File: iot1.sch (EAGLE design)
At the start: 10 parts, among them U2 HTU21D

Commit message: adding MEGA8-P controller
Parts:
- added C2, C3, C4: (no value), rcl:C-EU050-025X075
- added IC1: MEGA8-P, atmel:MEGA8-P
- added Q1: (no value), crystal:CRYSTALHC18U-V
- added R3, R4: (no value), rcl:R-EU_0204/7
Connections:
- new net 5V: C2.1, IC1.VCC@1, R3.2
- new net N$15: IC1.PC0(ADC0)
- new net N$16: IC1.PC1(ADC1)
- new net N$22: IC1.PC2(ADC2)
- new net N$23: IC1.PC3(ADC3)
- new net N$29: IC1.PC4(ADC4/SDA)
- new net N$31: IC1.PC5(ADC5/SCL)
- new net N$41: IC1.PD0(RXD)
- new net N$42: IC1.PD1(TXD)
- new net N$43: IC1.PD2(INT0)
- new net N$44: IC1.PD3(INT1)
- new net N$45: IC1.PD4(XCK/T0)
- new net N$58: IC1.PD5(T1)
- new net N$59: IC1.PD6(AIN0)
- new net N$60: IC1.PD7(AIN1)
- new net N$61: IC1.PB0(ICP)
- new net N$62: IC1.PB1(OC1A)
- new net N$63: IC1.PB2(SS/OC1B)
- new net N$64: IC1.PB3(MOSI/OC2)
- new net N$65: IC1.PB4(MISO)
- new net N$66: IC1.PB5(SCK)
- new net N$67: IC1.PC6(/RESET), R3.1
- new net N$68: IC1.GND
- new net N$69: IC1.AREF
- new net N$70: IC1.AVCC
- new net N$72: C4.2, IC1.PB7(XTAL2/TOSC2), Q1.1, R4.1
- new net N$73: C3.2, IC1.PB6(XTAL1/TOSC1), Q1.2, R4.2
- net GND: now also C2.2, C3.1, C4.1, IC1.GND@1

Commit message: adding moisture input and adding voltage regulator
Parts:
- added IC2: 7805T, linear:7805T
- added X1: 22-23-2041, con-molex:22-23-2041
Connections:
- removed net N$65: IC1.PB4(MISO)
- removed net N$66: IC1.PB5(SCK)
- new net SOIL_MOISTURE_0: X1-1.S
- new net SOIL_MOISTURE_1: X1-3.S
- new net V_IN: IC2.VI
- net 5V: now also IC2.VO
- net GND: now also IC2.GND, X1-2.S, X1-4.S
- net RX: now also IC1.PB4(MISO)
- net TX: now also IC1.PB5(SCK)
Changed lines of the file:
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@@
 <part name="C3" library="rcl" library_urn="urn:adsk.eagle:library:334" deviceset="C-EU" device="050-025X075" package3d_urn="urn:adsk.eagle:package:23637/1"/>
 <part name="C4" library="rcl" library_urn="urn:adsk.eagle:library:334" deviceset="C-EU" device="050-025X075" package3d_urn="urn:adsk.eagle:package:23637/1"/>
+<part name="FRAME4" library="frames" library_urn="urn:adsk.eagle:library:229" deviceset="A4L-LOC" device=""/>
+<part name="X1" library="con-molex" library_urn="urn:adsk.eagle:library:165" deviceset="22-23-2041" device="" package3d_urn="urn:adsk.eagle:package:8078635/1"/>
+<part name="IC2" library="linear" library_urn="urn:adsk.eagle:library:262" deviceset="78*" device="T" package3d_urn="urn:adsk.eagle:package:16414/1" technology="05"/>
 </parts>
 <sheets>
@@
 </segment>
 </net>
-<net name="N$65" class="0">
+<net name="RX" class="0">
 <segment>
 <pinref part="IC1" gate="G$1" pin="PB4(MISO)"/>
 <wire x1="162.56" y1="109.22" x2="187.96" y2="109.22" width="0.1524" layer="91"/>
-</segment>
-</net>
-<net name="N$66" class="0">
+<label x="190.5" y="109.22" size="1.778" layer="95"/>
+</segment>
+</net>
+<net name="TX" class="0">
 <segment>
 <pinref part="IC1" gate="G$1" pin="PB5(SCK)"/>
 <wire x1="162.56" y1="106.68" x2="187.96" y2="106.68" width="0.1524" layer="91"/>
+<label x="190.5" y="106.68" size="1.778" layer="95"/>
 </segment>
 </net>
@@
 </segment>
 </net>
+</nets>
+</sheet>
+<sheet>
+<plain>
+</plain>
+<instances>
+<instance part="FRAME4" gate="G$1" x="-5.08" y="10.16" smashed="yes">
+<attribute name="DRAWING_NAME" x="212.09" y="25.4" size="2.54" layer="94"/>
+<attribute name="LAST_DATE_TIME" x="212.09" y="20.32" size="2.286" layer="94"/>
+<attribute name="SHEET" x="225.425" y="15.24" size="2.54" layer="94"/>
+</instance>
+<instance part="X1" gate="-1" x="190.5" y="121.92" smashed="yes">
+<attribute name="NAME" x="193.04" y="121.158" size="1.524" layer="95"/>
+<attribute name="VALUE" x="189.738" y="123.317" size="1.778" layer="96"/>
+</instance>
+<instance part="X1" gate="-2" x="190.5" y="119.38" smashed="yes">
+<attribute name="NAME" x="193.04" y="118.618" size="1.524" layer="95"/>
+</instance>
+<instance part="X1" gate="-3" x="190.5" y="116.84" smashed="yes">
+<attribute name="NAME" x="193.04" y="116.078" size="1.524" layer="95"/>
+</instance>
+<instance part="X1" gate="-4" x="190.5" y="114.3" smashed="yes">
+<attribute name="NAME" x="193.04" y="113.538" size="1.524" layer="95"/>
+</instance>
+<instance part="IC2" gate="A1" x="55.88" y="142.24" smashed="yes">
+<attribute name="NAME" x="48.26" y="147.955" size="1.778" layer="95"/>
+<attribute name="VALUE" x="48.26" y="145.415" size="1.778" layer="96"/>
+</instance>
+</instances>
+<busses>
+</busses>
+<nets>
+<net name="SOIL_MOISTURE_0" class="0">
+<segment>
+<pinref part="X1" gate="-1" pin="S"/>
+<wire x1="187.96" y1="121.92" x2="177.8" y2="121.92" width="0.1524" layer="91"/>
+<label x="152.4" y="121.92" size="1.778" layer="95"/>
+</segment>
+</net>
+<net name="GND" class="0">
+<segment>
+<pinref part="X1" gate="-2" pin="S"/>
+<wire x1="187.96" y1="119.38" x2="177.8" y2="119.38" width="0.1524" layer="91"/>
+<label x="170.18" y="119.38" size="1.778" layer="95"/>
+</segment>
+<segment>
+<pinref part="X1" gate="-4" pin="S"/>
+<wire x1="187.96" y1="114.3" x2="177.8" y2="114.3" width="0.1524" layer="91"/>
+<label x="170.18" y="114.3" size="1.778" layer="95"/>
+</segment>
+<segment>
+<pinref part="IC2" gate="A1" pin="GND"/>
+<wire x1="55.88" y1="134.62" x2="55.88" y2="129.54" width="0.1524" layer="91"/>
+<label x="55.88" y="127" size="1.778" layer="95"/>
+</segment>
+</net>
+<net name="SOIL_MOISTURE_1" class="0">
+<segment>
+<pinref part="X1" gate="-3" pin="S"/>
+<wire x1="187.96" y1="116.84" x2="177.8" y2="116.84" width="0.1524" layer="91"/>
+<label x="152.4" y="116.84" size="1.778" layer="95"/>
+</segment>
+</net>
+<net name="V_IN" class="0">
+<segment>
+<pinref part="IC2" gate="A1" pin="VI"/>
+<wire x1="45.72" y1="142.24" x2="43.18" y2="142.24" width="0.1524" layer="91"/>
+<label x="35.56" y="142.24" size="1.778" layer="95"/>
+</segment>
+</net>
+<net name="5V" class="0">
+<segment>
+<pinref part="IC2" gate="A1" pin="VO"/>
+<wire x1="66.04" y1="142.24" x2="71.12" y2="142.24" width="0.1524" layer="91"/>
+<label x="73.66" y="142.24" size="1.778" layer="95"/>
+</segment>
+</net>

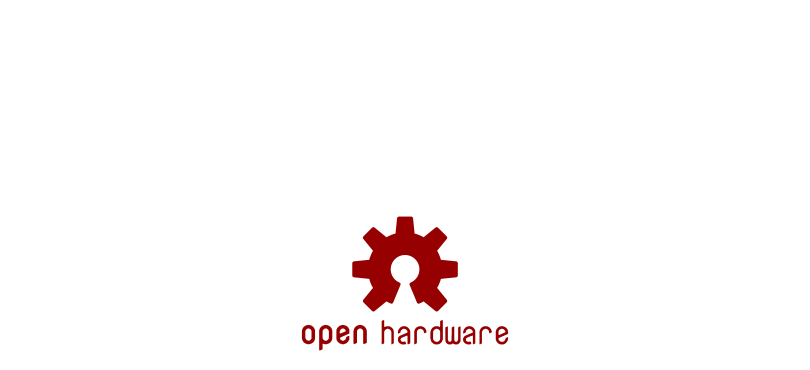
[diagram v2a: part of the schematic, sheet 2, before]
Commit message: adding power supply
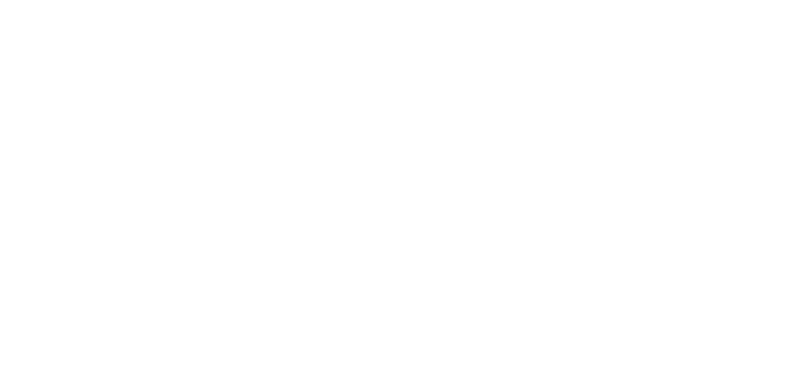
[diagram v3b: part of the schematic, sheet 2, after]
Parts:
- removed LOGO2: OSHW-LOGOS, SparkFun-Aesthetics:OSHW-LOGOS
- added C5, C6: (no value), rcl:CPOL-EUE1.8-4
- added J1: DCJ0202, con-jack:DCJ0202
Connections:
- net 5V: now also C6.+
- net GND: now also C5.-, C6.-, J1.2, J1.3
- net V_IN: now also C5.+, J1.1
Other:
- moved on the sheet: IC2
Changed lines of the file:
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@@
 <part name="GND4" library="SparkFun" deviceset="GND" device=""/>
 <part name="U2" library="SparkFun-Sensors" deviceset="HTU21D" device="SMD" value="HTU21D"/>
-<part name="LOGO2" library="SparkFun-Aesthetics" deviceset="OSHW-LOGO" device="S"/>
 <part name="JP1" library="SparkFun-Connectors" deviceset="M04" device="PTH"/>
 <part name="GND2" library="SparkFun" deviceset="GND" device=""/>
@@
 <part name="X1" library="con-molex" library_urn="urn:adsk.eagle:library:165" deviceset="22-23-2041" device="" package3d_urn="urn:adsk.eagle:package:8078635/1"/>
 <part name="IC2" library="linear" library_urn="urn:adsk.eagle:library:262" deviceset="78*" device="T" package3d_urn="urn:adsk.eagle:package:16414/1" technology="05"/>
+<part name="J1" library="con-jack" library_urn="urn:adsk.eagle:library:154" deviceset="DCJ0202" device="" package3d_urn="urn:adsk.eagle:package:7491/1"/>
+<part name="C5" library="rcl" library_urn="urn:adsk.eagle:library:334" deviceset="CPOL-EU" device="E1.8-4" package3d_urn="urn:adsk.eagle:package:23336/2"/>
+<part name="C6" library="rcl" library_urn="urn:adsk.eagle:library:334" deviceset="CPOL-EU" device="E1.8-4" package3d_urn="urn:adsk.eagle:package:23336/2"/>
 </parts>
 <sheets>
@@
 <attribute name="VALUE" x="139.7" y="78.74" size="1.778" layer="95"/>
 </instance>
-<instance part="LOGO2" gate="G$1" x="134.62" y="10.16" smashed="yes"/>
 <instance part="JP1" gate="G$1" x="73.66" y="96.52" smashed="yes" rot="MR180">
 <attribute name="VALUE" x="68.58" y="104.14" size="1.778" layer="96" rot="MR180"/>
@@
 <attribute name="NAME" x="193.04" y="113.538" size="1.524" layer="95"/>
 </instance>
-<instance part="IC2" gate="A1" x="55.88" y="142.24" smashed="yes">
-<attribute name="NAME" x="48.26" y="147.955" size="1.778" layer="95"/>
-<attribute name="VALUE" x="48.26" y="145.415" size="1.778" layer="96"/>
+<instance part="IC2" gate="A1" x="50.8" y="142.24" smashed="yes">
+<attribute name="NAME" x="43.18" y="147.955" size="1.778" layer="95"/>
+<attribute name="VALUE" x="43.18" y="145.415" size="1.778" layer="96"/>
+</instance>
+<instance part="J1" gate="G$1" x="12.7" y="139.7" smashed="yes">
+<attribute name="NAME" x="10.16" y="143.51" size="1.778" layer="95"/>
+<attribute name="VALUE" x="10.16" y="133.35" size="1.778" layer="96"/>
+</instance>
+<instance part="C5" gate="G$1" x="33.02" y="137.16" smashed="yes">
+<attribute name="NAME" x="34.163" y="137.6426" size="1.778" layer="95"/>
+<attribute name="VALUE" x="34.163" y="132.5626" size="1.778" layer="96"/>
+</instance>
+<instance part="C6" gate="G$1" x="68.58" y="134.62" smashed="yes">
+<attribute name="NAME" x="69.723" y="135.1026" size="1.778" layer="95"/>
+<attribute name="VALUE" x="69.723" y="130.0226" size="1.778" layer="96"/>
 </instance>
 </instances>
@@
 <segment>
 <pinref part="IC2" gate="A1" pin="GND"/>
-<wire x1="55.88" y1="134.62" x2="55.88" y2="129.54" width="0.1524" layer="91"/>
-<label x="55.88" y="127" size="1.778" layer="95"/>
+<wire x1="50.8" y1="134.62" x2="50.8" y2="127" width="0.1524" layer="91"/>
+<label x="55.88" y="124.46" size="1.778" layer="95"/>
+<wire x1="25.4" y1="127" x2="33.02" y2="127" width="0.1524" layer="91"/>
+<pinref part="C5" gate="G$1" pin="-"/>
+<wire x1="33.02" y1="127" x2="33.02" y2="132.08" width="0.1524" layer="91"/>
+<wire x1="33.02" y1="127" x2="50.8" y2="127" width="0.1524" layer="91"/>
+<junction x="33.02" y="127"/>
+<pinref part="C6" gate="G$1" pin="-"/>
+<wire x1="68.58" y1="129.54" x2="68.58" y2="127" width="0.1524" layer="91"/>
+<wire x1="68.58" y1="127" x2="50.8" y2="127" width="0.1524" layer="91"/>
+<junction x="50.8" y="127"/>
+<pinref part="J1" gate="G$1" pin="2"/>
+<wire x1="20.32" y1="139.7" x2="25.4" y2="139.7" width="0.1524" layer="91"/>
+<wire x1="25.4" y1="137.16" x2="25.4" y2="139.7" width="0.1524" layer="91"/>
+<pinref part="J1" gate="G$1" pin="3"/>
+<wire x1="20.32" y1="137.16" x2="25.4" y2="137.16" width="0.1524" layer="91"/>
+<wire x1="25.4" y1="137.16" x2="25.4" y2="127" width="0.1524" layer="91"/>
+<junction x="25.4" y="137.16"/>
 </segment>
 </net>
@@
 <segment>
 <pinref part="IC2" gate="A1" pin="VI"/>
-<wire x1="45.72" y1="142.24" x2="43.18" y2="142.24" width="0.1524" layer="91"/>
-<label x="35.56" y="142.24" size="1.778" layer="95"/>
+<pinref part="J1" gate="G$1" pin="1"/>
+<wire x1="20.32" y1="142.24" x2="33.02" y2="142.24" width="0.1524" layer="91"/>
+<pinref part="C5" gate="G$1" pin="+"/>
+<wire x1="33.02" y1="142.24" x2="33.02" y2="139.7" width="0.1524" layer="91"/>
+<wire x1="33.02" y1="142.24" x2="40.64" y2="142.24" width="0.1524" layer="91"/>
+<junction x="33.02" y="142.24"/>
 </segment>
 </net>
@@
 <segment>
 <pinref part="IC2" gate="A1" pin="VO"/>
-<wire x1="66.04" y1="142.24" x2="71.12" y2="142.24" width="0.1524" layer="91"/>
 <label x="73.66" y="142.24" size="1.778" layer="95"/>
-</segment>
-</net>
+<pinref part="C6" gate="G$1" pin="+"/>
+<wire x1="60.96" y1="142.24" x2="68.58" y2="142.24" width="0.1524" layer="91"/>
+<wire x1="68.58" y1="142.24" x2="68.58" y2="137.16" width="0.1524" layer="91"/>
+</segment>
+</net>

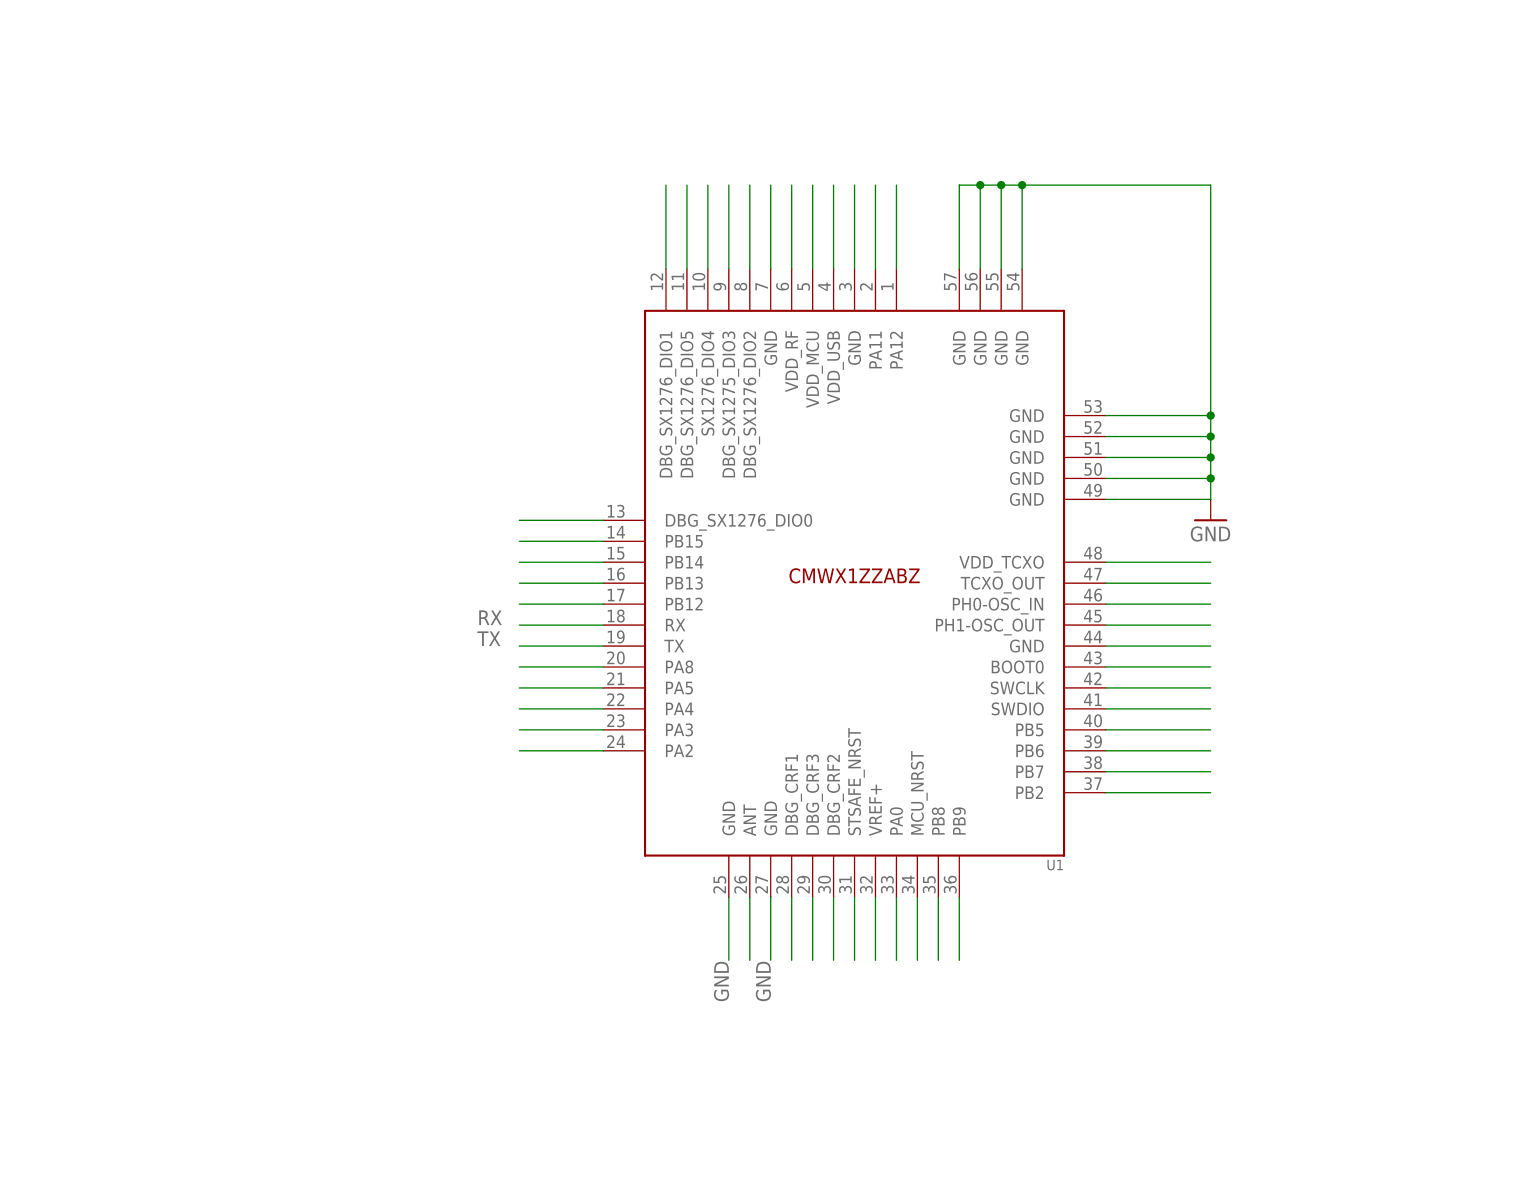
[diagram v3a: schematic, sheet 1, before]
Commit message: antena, power supply y conexiones lorawan
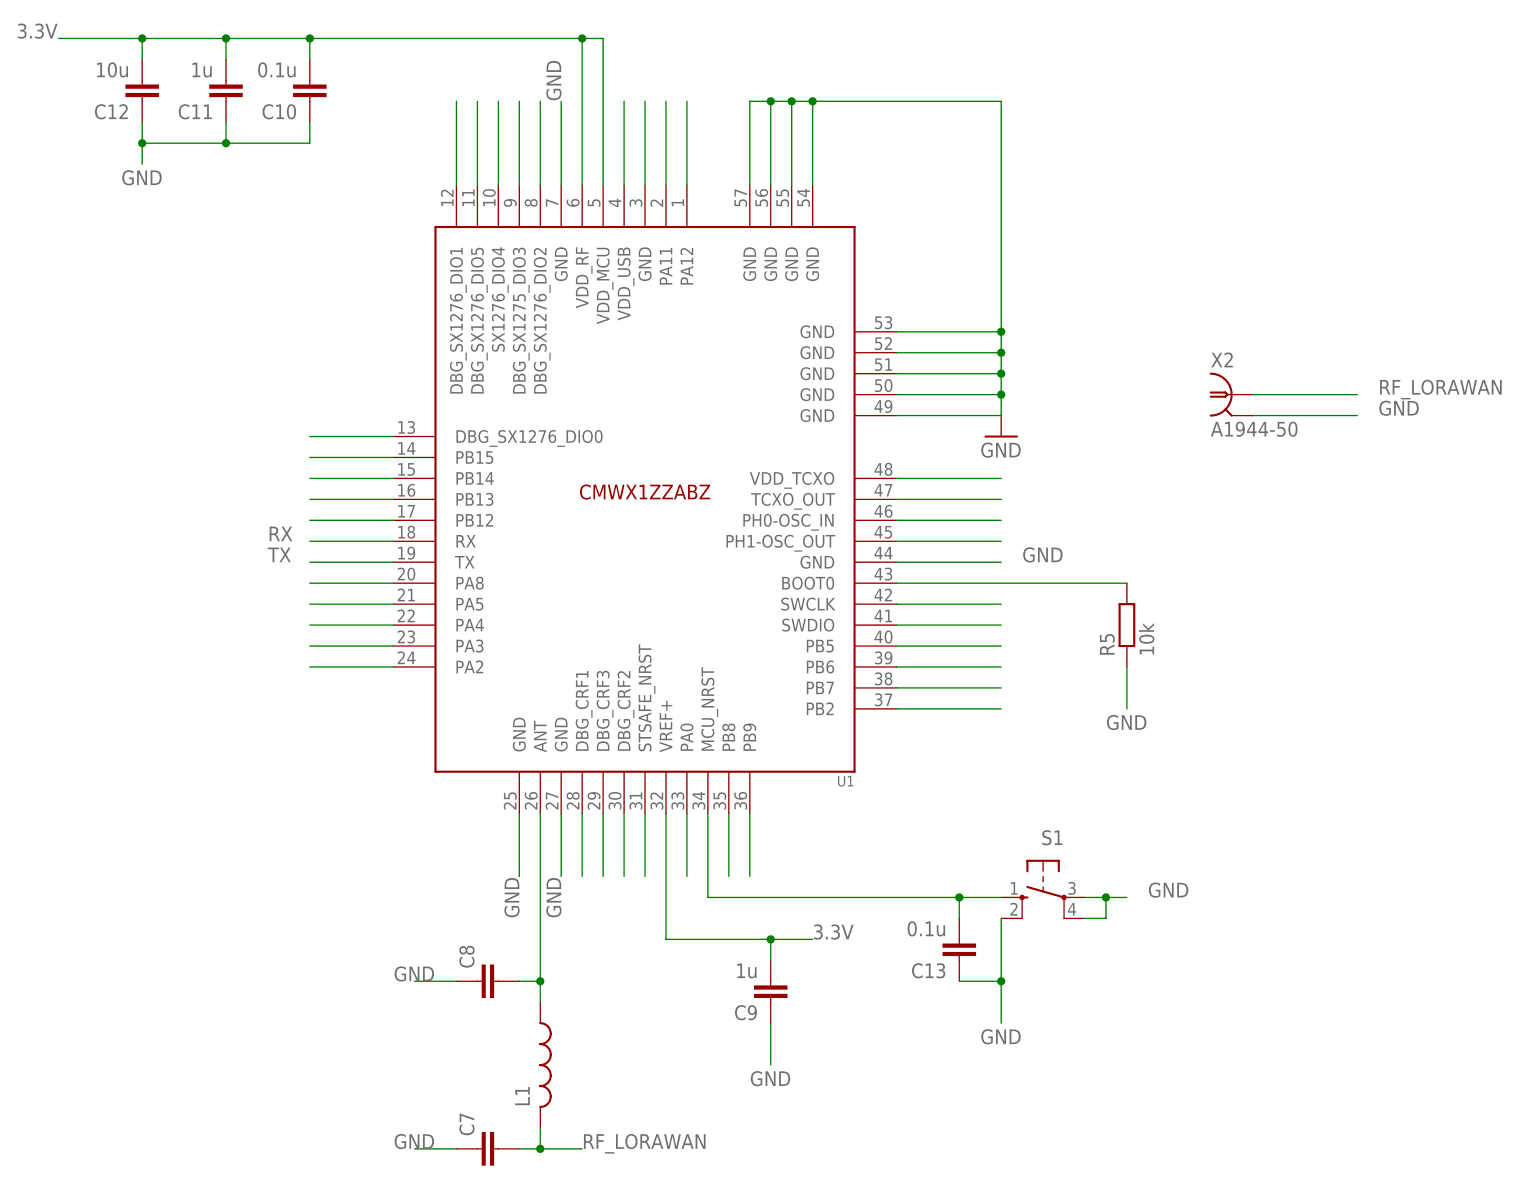
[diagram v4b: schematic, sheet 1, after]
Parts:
- added C10, C13: 0.1u, rcl:C-EU050-025X075
- added C11, C9: 1u, rcl:C-EU050-025X075
- added C12: 10u, rcl:C-EU050-025X075
- added C7, C8: (no value), rcl:C-EU050-025X075
- added L1: (no value), rcl:L-US0207/7
- added R5: 10k, rcl:R-EU_0204/5
- added S1: (no value), switch-omron:10-XX
- added X2: A1944-50, con-coax:A1944-50
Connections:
- removed net N$36: U1.VREF+
- removed net N$50: U1.GND@44
- removed net N$6 (its old number): U1.GND@7
- removed net N$7: U1.VDD_RF
- removed net N$8: U1.VDD_MCU
- new net RF_LORAWAN: C7.2, L1.2, X2.1
- net 3.3V: now also C10.2, C11.2, C12.2, C9.2, U1.VDD_MCU, U1.VDD_RF, U1.VREF+
- net GND: now also C10.1, C11.1, C12.1, C13.1, C7.1, C8.1, C9.1, R5.1, S1.P, S1.P1, S1.S1, U1.GND@44, U1.GND@7, X2.2
- net N$30: now also C8.2, L1.1
- net N$38: now also C13.2, S1.S
- net N$51: now also R5.2
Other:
- moved on the sheet: U1
